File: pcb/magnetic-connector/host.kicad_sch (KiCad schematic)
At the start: 8 parts

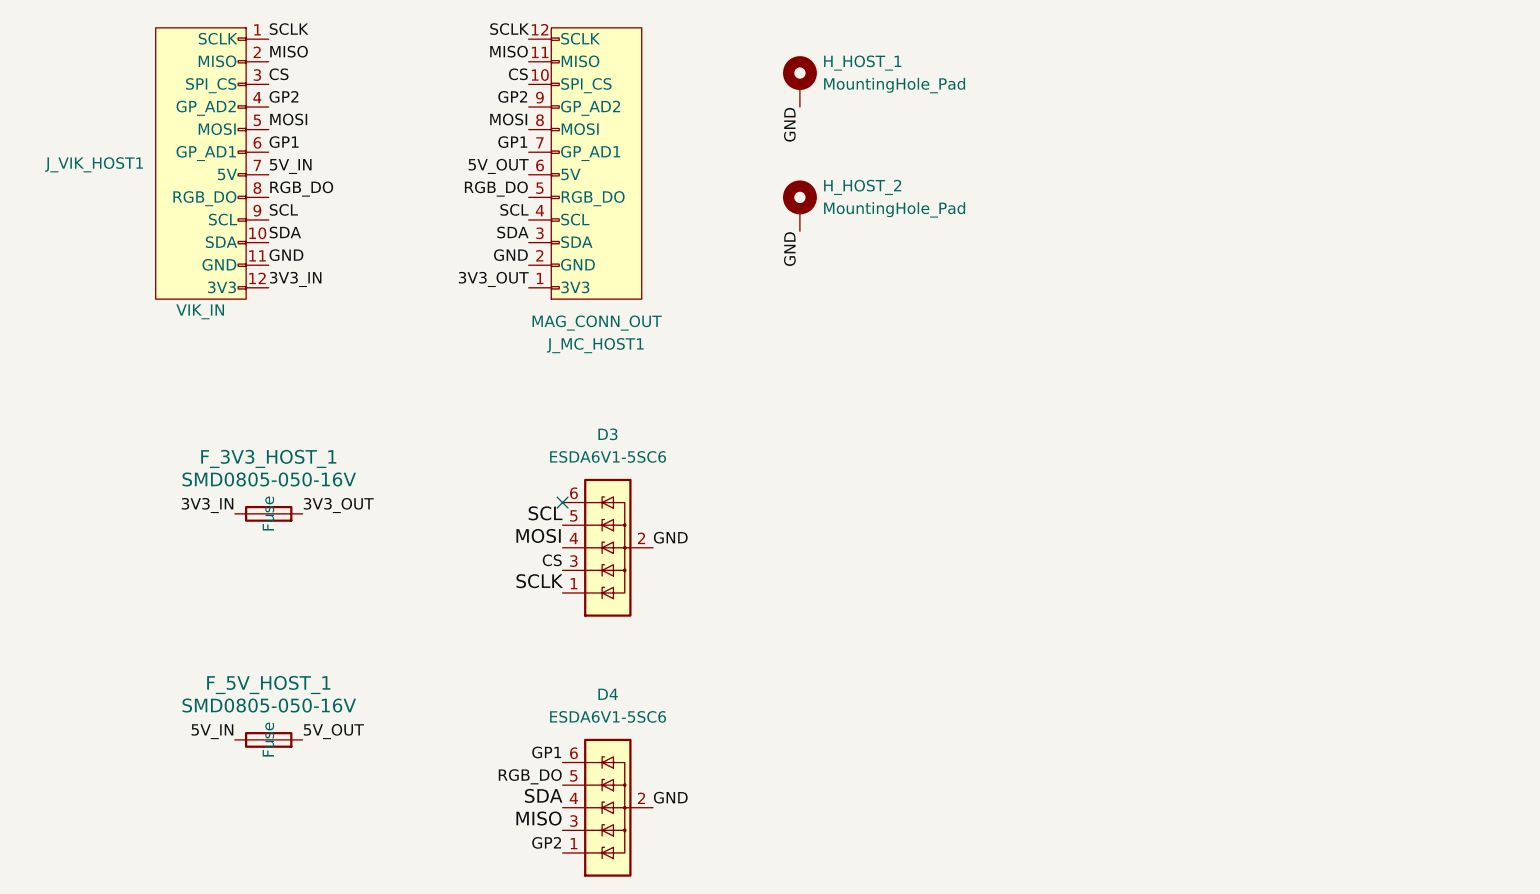
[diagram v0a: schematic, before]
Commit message: Change ESD protection chips on magnetic connector.
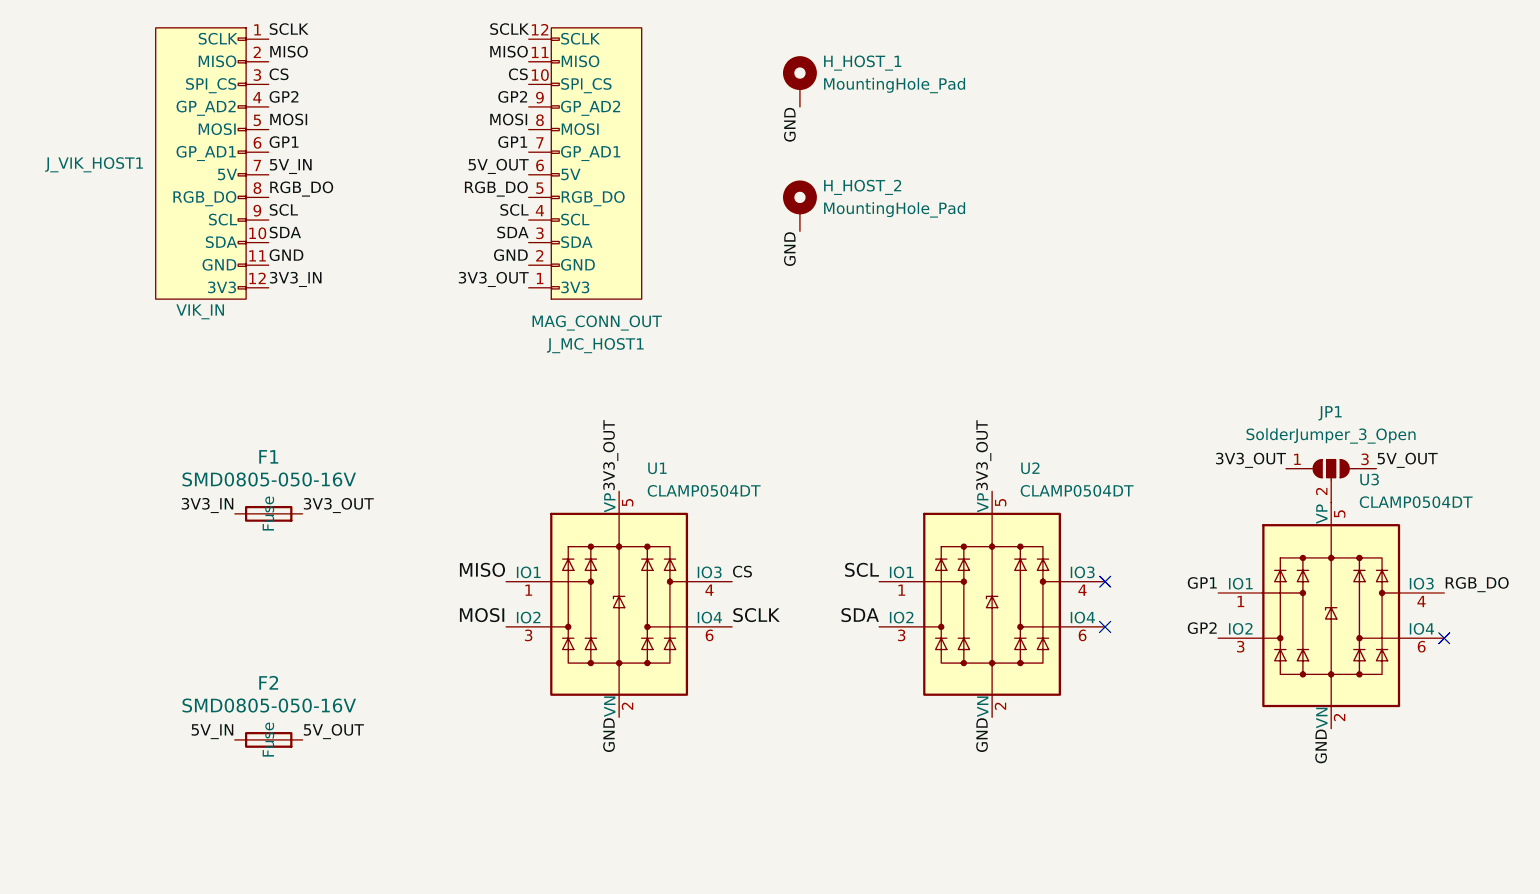
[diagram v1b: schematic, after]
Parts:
- removed D3, D4: ESDA6V1-5SC6, Package_TO_SOT_SMD:SOT-23-6, symbol Power_Protection:ESDA6V1-5SC6
- added JP1: SolderJumper_3_Open, Jumper:SolderJumper-3_P2.0mm_Open_TrianglePad1.0x1.5mm_NumberLabels, symbol Jumper:SolderJumper_3_Open
- added U1, U2, U3: CLAMP0504DT, Package_TO_SOT_SMD:SOT-23-6, symbol Power_Protection:SRV05-4
- J_VIK_HOST1: LCSC (none) -> C2856799
- renumbered F_3V3_HOST_1 to F1, F_5V_HOST_1 to F2
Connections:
- net 3V3_OUT: now also JP1.1 (A), U1.5 (VP), U2.5 (VP)
- net 5V_OUT: now also JP1.3 (B)
- net CS: now also U1.4 (IO3)
- net GND: now also U1.2 (VN), U2.2 (VN), U3.2 (VN)
- net GP1: now also U3.1 (IO1)
- net GP2: now also U3.3 (IO2)
- net MISO: now also U1.1 (IO1)
- net MOSI: now also U1.3 (IO2)
- net RGB_DO: now also U3.4 (IO3)
- net SCL: now also U2.1 (IO1)
- net SCLK: now also U1.6 (IO4)
- net SDA: now also U2.3 (IO2)
- new net: JP1.2 (C), U3.5 (VP)
- no-connect marks 1 -> 3
